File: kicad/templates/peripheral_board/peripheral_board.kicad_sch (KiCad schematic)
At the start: 6 parts, among them J1 peripheral_addr_bus_connector, J2 peripheral_aux_connector, J3 peripheral_membank_connector

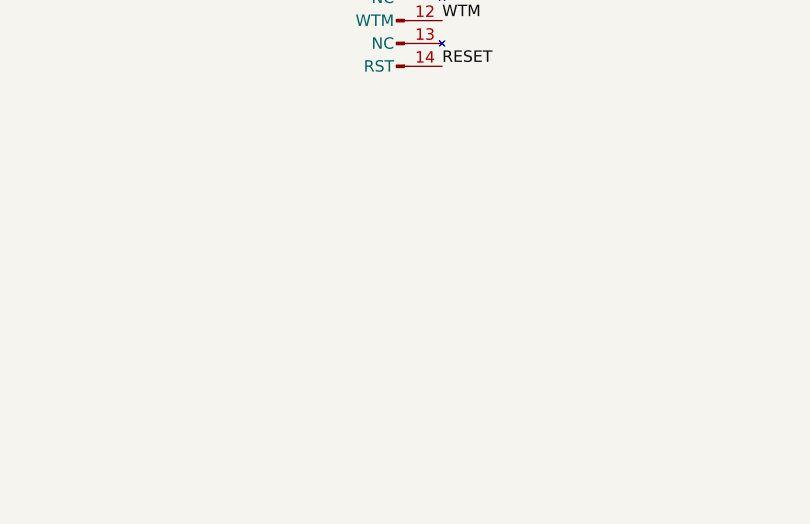
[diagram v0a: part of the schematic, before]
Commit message: Add resistor, capacitor and test points to periperal template.
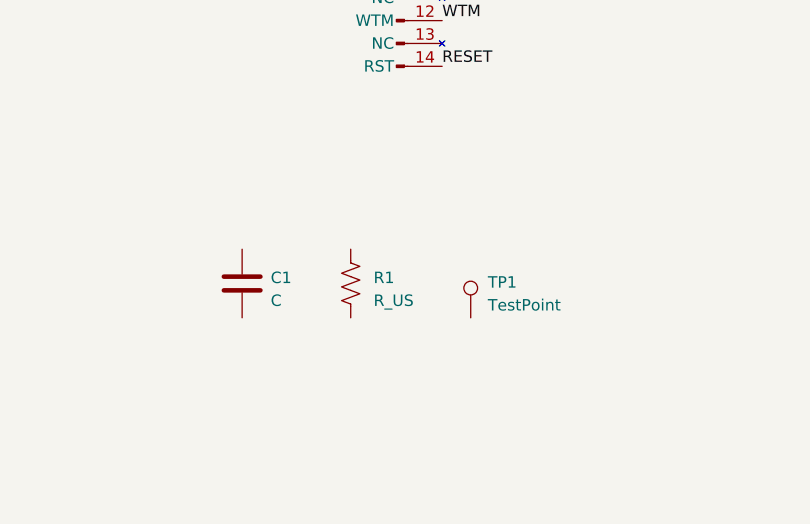
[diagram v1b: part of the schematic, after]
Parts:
- added C1: C, Capacitor_THT:C_Disc_D5.0mm_W2.5mm_P5.00mm, symbol Device:C
- added R1: R_US, Resistor_THT:R_Axial_DIN0207_L6.3mm_D2.5mm_P10.16mm_Horizontal, symbol Device:R_US
- added TP1: TestPoint, Connector_Pin:Pin_D1.0mm_L10.0mm, symbol Connector:TestPoint
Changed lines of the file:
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@@
 (kicad_sch (version 20230121) (generator eeschema)
   (paper "B")
+  (bus_alias "ADDR_BUS" (members "ADDR_BUS_00" "ADDR_BUS_01" "ADDR_BUS_02" "ADDR_BUS_03" "ADDR_BUS_04" "ADDR_BUS_05" "ADDR_BUS_06" "ADDR_BUS_07" "ADDR_BUS_08" "ADDR_BUS_09" "ADDR_BUS_10" "ADDR_BUS_11" "ADDR_BUS_12" "ADDR_BUS_13" "ADDR_BUS_14" "ADDR_BUS_15"))
+  (bus_alias "DATA_BUS" (members "DATA_BUS_00" "DATA_BUS_01" "DATA_BUS_02" "DATA_BUS_03" "DATA_BUS_04" "DATA_BUS_05" "DATA_BUS_06" "DATA_BUS_07" "DATA_BUS_08" "DATA_BUS_09" "DATA_BUS_10" "DATA_BUS_11" "DATA_BUS_12" "DATA_BUS_13" "DATA_BUS_14" "DATA_BUS_15"))
   (bus_alias "BANK_BUS" (members "BANK_BUS_00" "BANK_BUS_01" "BANK_BUS_02" "BANK_BUS_03" "BANK_BUS_04" "BANK_BUS_05" "BANK_BUS_06" "BANK_BUS_07" "BANK_BUS_08" "BANK_BUS_09" "BANK_BUS_10" "BANK_BUS_11" "BANK_BUS_12" "BANK_BUS_13" "BANK_BUS_14" "BANK_BUS_15"))
-  (bus_alias "DATA_BUS" (members "DATA_BUS_00" "DATA_BUS_01" "DATA_BUS_02" "DATA_BUS_03" "DATA_BUS_04" "DATA_BUS_05" "DATA_BUS_06" "DATA_BUS_07" "DATA_BUS_08" "DATA_BUS_09" "DATA_BUS_10" "DATA_BUS_11" "DATA_BUS_12" "DATA_BUS_13" "DATA_BUS_14" "DATA_BUS_15"))
-  (bus_alias "ADDR_BUS" (members "ADDR_BUS_00" "ADDR_BUS_01" "ADDR_BUS_02" "ADDR_BUS_03" "ADDR_BUS_04" "ADDR_BUS_05" "ADDR_BUS_06" "ADDR_BUS_07" "ADDR_BUS_08" "ADDR_BUS_09" "ADDR_BUS_10" "ADDR_BUS_11" "ADDR_BUS_12" "ADDR_BUS_13" "ADDR_BUS_14" "ADDR_BUS_15"))
   (junction (at 377.19 33.655) (diameter 0) (color 0 0 0 0)
   )
@@
         (path "/0c25b387-1696-4e3f-ab8e-df646088b074"
           (reference "C99") (unit 1)
+        )
+      )
+    )
+  )
+  (symbol (lib_id "Connector:TestPoint") (at 117.475 86.36 0) (unit 1)
+    (in_bom yes) (on_board yes) (dnp no) (fields_autoplaced)
+    (property "Reference" "TP1" (at 119.38 82.423 0)
+      (effects (font (size 1.27 1.27)) (justify left))
+    )
+    (property "Value" "TestPoint" (at 119.38 84.963 0)
+      (effects (font (size 1.27 1.27)) (justify left))
+    )
+    (property "Footprint" "Connector_Pin:Pin_D1.0mm_L10.0mm" (at 122.555 86.36 0)
+      (effects (font (size 1.27 1.27)) hide)
+    )
+    (property "Datasheet" "~" (at 122.555 86.36 0)
+      (effects (font (size 1.27 1.27)) hide)
+    )
+    (pin "1")
+    (instances
+      (project "peripheral_board"
+        (path "/0c25b387-1696-4e3f-ab8e-df646088b074"
+          (reference "TP1") (unit 1)
         )
       )
@@
     )
   )
+  (symbol (lib_id "Device:C") (at 92.075 82.55 0) (unit 1)
+    (in_bom yes) (on_board yes) (dnp no) (fields_autoplaced)
+    (property "Reference" "C1" (at 95.25 81.915 0)
+      (effects (font (size 1.27 1.27)) (justify left))
+    )
+    (property "Value" "C" (at 95.25 84.455 0)
+      (effects (font (size 1.27 1.27)) (justify left))
+    )
+    (property "Footprint" "Capacitor_THT:C_Disc_D5.0mm_W2.5mm_P5.00mm" (at 93.0402 86.36 0)
+      (effects (font (size 1.27 1.27)) hide)
+    )
+    (property "Datasheet" "~" (at 92.075 82.55 0)
+      (effects (font (size 1.27 1.27)) hide)
+    )
+    (pin "1")
+    (pin "2")
+    (instances
+      (project "peripheral_board"
+        (path "/0c25b387-1696-4e3f-ab8e-df646088b074"
+          (reference "C1") (unit 1)
+        )
+      )
+    )
+  )
   (symbol (lib_id "power:PWR_FLAG") (at 342.9 33.655 180) (unit 1)
     (in_bom yes) (on_board yes) (dnp no) (fields_autoplaced)
@@
         )
       )
+    )
+  )
+  (symbol (lib_id "Device:R_US") (at 104.14 82.55 0) (unit 1)
+    (in_bom yes) (on_board yes) (dnp no) (fields_autoplaced)
+    (property "Reference" "R1" (at 106.68 81.915 0)
+      (effects (font (size 1.27 1.27)) (justify left))
+    )
+    (property "Value" "R_US" (at 106.68 84.455 0)
+      (effects (font (size 1.27 1.27)) (justify left))
+    )
+    (property "Footprint" "Resistor_THT:R_Axial_DIN0207_L6.3mm_D2.5mm_P10.16mm_Horizontal" (at 105.156 82.804 90)
+      (effects (font (size 1.27 1.27)) hide)
+    )
+    (property "Datasheet" "~" (at 104.14 82.55 0)
+      (effects (font (size 1.27 1.27)) hide)
+    )
+    (pin "1")
+    (pin "2")
+    (instances
+      (project "peripheral_board"
+        (path "/0c25b387-1696-4e3f-ab8e-df646088b074"
+          (reference "R1") (unit 1)
+        )
+      )
